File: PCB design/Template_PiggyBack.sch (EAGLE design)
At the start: 46 parts, among them CN1 USB power supply, IC1 MCP6002, IC3 MCP6002, IC4 REG1117

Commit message: PCB Output
changed the PCB Output to PC1 and PC3
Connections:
- removed net PA4: R12.2, TP3.TP
- net PA5: no longer R6.2, TP4.TP
- net PC1_: now also R6.2, TP4.TP
- net PC3: now also R12.2, TP3.TP
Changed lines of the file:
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@@
 <label x="27.94" y="86.36" size="1.778" layer="95"/>
-</segment>
-</net>
-<net name="PC3" class="0">
-<segment>
-<pinref part="J2" gate="G$1" pin="8"/>
-<wire x1="35.56" y1="83.82" x2="33.02" y2="83.82" width="0.1524" layer="91"/>
-<label x="27.94" y="83.82" size="1.778" layer="95"/>
-</segment>
-</net>
-<net name="PA5" class="0">
-<segment>
-<pinref part="J2" gate="G$1" pin="11"/>
-<wire x1="35.56" y1="76.2" x2="33.02" y2="76.2" width="0.1524" layer="91"/>
-<label x="27.94" y="76.2" size="1.778" layer="95"/>
 </segment>
 <segment>
@@
 <wire x1="259.08" y1="-66.04" x2="264.16" y2="-66.04" width="0.1524" layer="91"/>
 <junction x="259.08" y="-66.04"/>
+</segment>
+</net>
+<net name="PC3" class="0">
+<segment>
+<pinref part="J2" gate="G$1" pin="8"/>
+<wire x1="35.56" y1="83.82" x2="33.02" y2="83.82" width="0.1524" layer="91"/>
+<label x="27.94" y="83.82" size="1.778" layer="95"/>
+</segment>
+<segment>
+<pinref part="R12" gate="G$1" pin="2"/>
+<wire x1="256.54" y1="-205.74" x2="261.62" y2="-205.74" width="0.1524" layer="91"/>
+<pinref part="TP3" gate="G$1" pin="TP"/>
+<wire x1="261.62" y1="-205.74" x2="266.7" y2="-205.74" width="0.1524" layer="91"/>
+<junction x="261.62" y="-205.74"/>
+<label x="269.24" y="-205.74" size="1.778" layer="95"/>
+</segment>
+</net>
+<net name="PA5" class="0">
+<segment>
+<pinref part="J2" gate="G$1" pin="11"/>
+<wire x1="35.56" y1="76.2" x2="33.02" y2="76.2" width="0.1524" layer="91"/>
+<label x="27.94" y="76.2" size="1.778" layer="95"/>
 </segment>
 <segment>
@@
 </segment>
 </net>
-<net name="PA4" class="0">
-<segment>
-<pinref part="R12" gate="G$1" pin="2"/>
-<wire x1="256.54" y1="-205.74" x2="261.62" y2="-205.74" width="0.1524" layer="91"/>
-<pinref part="TP3" gate="G$1" pin="TP"/>
-<wire x1="261.62" y1="-205.74" x2="266.7" y2="-205.74" width="0.1524" layer="91"/>
-<junction x="261.62" y="-205.74"/>
-<label x="269.24" y="-205.74" size="1.778" layer="95"/>
-</segment>
-</net>

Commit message: finished layout but it is subject to revision
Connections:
- net VCO: no longer R15.2
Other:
- moved on the sheet: R15
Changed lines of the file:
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@@
 <attribute name="VALUE" x="65.024" y="-134.239" size="1.778" layer="96"/>
 </instance>
-<instance part="R15" gate="G$1" x="81.28" y="-119.38" smashed="yes" rot="R180">
-<attribute name="NAME" x="85.09" y="-120.8786" size="1.778" layer="95" rot="R180"/>
-<attribute name="VALUE" x="85.09" y="-116.078" size="1.778" layer="96" rot="R180"/>
+<instance part="R15" gate="G$1" x="58.42" y="-119.38" smashed="yes" rot="R180">
+<attribute name="NAME" x="62.23" y="-120.8786" size="1.778" layer="95" rot="R180"/>
+<attribute name="VALUE" x="62.23" y="-116.078" size="1.778" layer="96" rot="R180"/>
 </instance>
 <instance part="GND1" gate="1" x="71.12" y="-137.16" smashed="yes">
@@
 <segment>
 <pinref part="R15" gate="G$1" pin="1"/>
-<wire x1="86.36" y1="-119.38" x2="96.52" y2="-119.38" width="0.1524" layer="91"/>
-<label x="96.52" y="-121.92" size="1.778" layer="95"/>
+<wire x1="63.5" y1="-119.38" x2="96.52" y2="-119.38" width="0.1524" layer="91"/>
 </segment>
 </net>
@@
 <pinref part="C17" gate="G$1" pin="1"/>
 <wire x1="71.12" y1="-127" x2="71.12" y2="-119.38" width="0.1524" layer="91"/>
-<pinref part="R15" gate="G$1" pin="2"/>
-<wire x1="71.12" y1="-119.38" x2="76.2" y2="-119.38" width="0.1524" layer="91"/>
-<wire x1="71.12" y1="-119.38" x2="60.96" y2="-119.38" width="0.1524" layer="91"/>
-<junction x="71.12" y="-119.38"/>
-<label x="55.88" y="-119.38" size="1.778" layer="95"/>
-</segment>
-</net>
+</segment>
+</net>

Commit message: better layout version
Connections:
- net PA5: now also R15.2; no longer R15.1
- net VCO: now also R15.1
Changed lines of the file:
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@@
 </segment>
 <segment>
-<pinref part="R15" gate="G$1" pin="1"/>
-<wire x1="63.5" y1="-119.38" x2="96.52" y2="-119.38" width="0.1524" layer="91"/>
+<pinref part="R15" gate="G$1" pin="2"/>
+<wire x1="53.34" y1="-119.38" x2="43.18" y2="-119.38" width="0.1524" layer="91"/>
+<label x="40.64" y="-116.84" size="1.778" layer="95"/>
 </segment>
 </net>
@@
 <pinref part="C17" gate="G$1" pin="1"/>
 <wire x1="71.12" y1="-127" x2="71.12" y2="-119.38" width="0.1524" layer="91"/>
-</segment>
-</net>
+<pinref part="R15" gate="G$1" pin="1"/>
+<wire x1="63.5" y1="-119.38" x2="71.12" y2="-119.38" width="0.1524" layer="91"/>
+<wire x1="71.12" y1="-119.38" x2="81.28" y2="-119.38" width="0.1524" layer="91"/>
+<junction x="71.12" y="-119.38"/>
+<label x="83.82" y="-116.84" size="1.778" layer="95"/>
+</segment>
+</net>

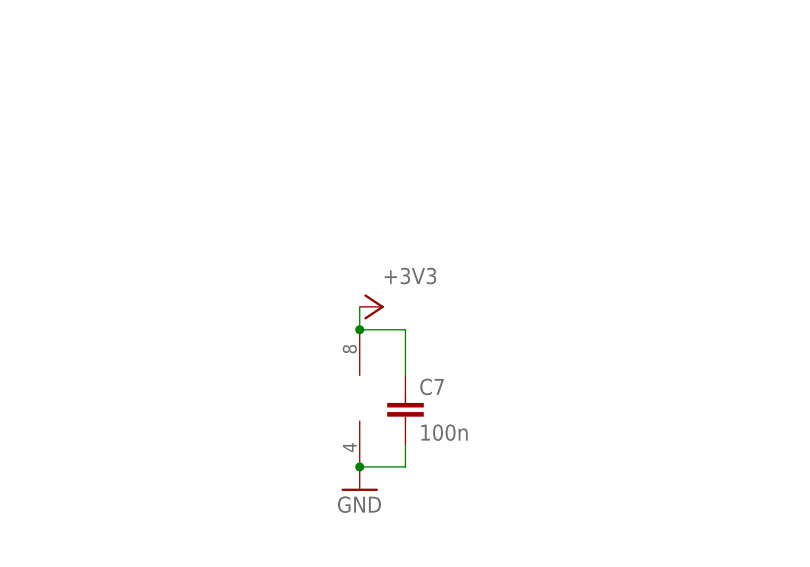
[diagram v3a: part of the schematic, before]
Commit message: errors in layout fixed
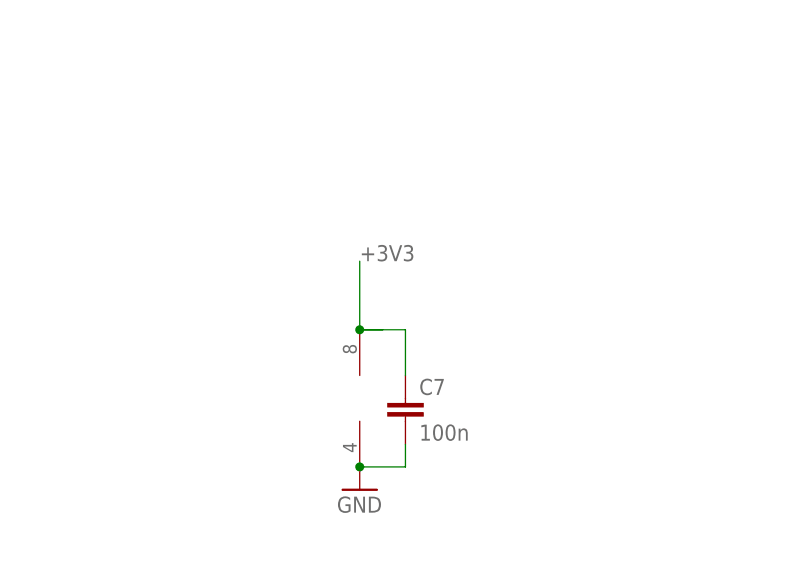
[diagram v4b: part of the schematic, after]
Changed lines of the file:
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@@
 <part name="TP6" library="testpad" library_urn="urn:adsk.eagle:library:385" deviceset="PTR1" device="PAD1-17" package3d_urn="urn:adsk.eagle:package:27949/1"/>
 <part name="+3V3" library="supply1" library_urn="urn:adsk.eagle:library:371" deviceset="+3V3" device=""/>
-<part name="+3V4" library="supply1" library_urn="urn:adsk.eagle:library:371" deviceset="+3V3" device=""/>
 <part name="C17" library="rcl" library_urn="urn:adsk.eagle:library:334" deviceset="C-EU" device="C0805" package3d_urn="urn:adsk.eagle:package:23617/2" value="1u"/>
 <part name="R15" library="rcl" library_urn="urn:adsk.eagle:library:334" deviceset="R-EU_" device="R0805" package3d_urn="urn:adsk.eagle:package:23553/2" value="3k"/>
@@
 <attribute name="VALUE" x="-7.62" y="-154.94" size="1.778" layer="96" rot="R180"/>
 </instance>
-<instance part="+3V4" gate="G$1" x="170.18" y="-27.94" smashed="yes" rot="R270">
-<attribute name="VALUE" x="170.18" y="-25.4" size="1.778" layer="96"/>
-</instance>
 <instance part="C17" gate="G$1" x="71.12" y="-129.54" smashed="yes">
 <attribute name="NAME" x="65.024" y="-129.159" size="1.778" layer="95"/>
@@
 </segment>
 <segment>
+<wire x1="170.18" y1="-162.56" x2="170.18" y2="-165.1" width="0.1524" layer="91"/>
+<label x="170.18" y="-162.56" size="1.778" layer="95"/>
+</segment>
+<segment>
 <pinref part="IC1" gate="P" pin="V+"/>
 <pinref part="C7" gate="G$1" pin="1"/>
 <wire x1="172.72" y1="-35.56" x2="172.72" y2="-30.48" width="0.1524" layer="91"/>
 <wire x1="172.72" y1="-30.48" x2="167.64" y2="-30.48" width="0.1524" layer="91"/>
-<wire x1="167.64" y1="-30.48" x2="167.64" y2="-27.94" width="0.1524" layer="91"/>
+<wire x1="167.64" y1="-30.48" x2="170.18" y2="-30.48" width="0.1524" layer="91"/>
 <junction x="167.64" y="-30.48"/>
-<pinref part="+3V4" gate="G$1" pin="+3V3"/>
-</segment>
-<segment>
-<wire x1="170.18" y1="-162.56" x2="170.18" y2="-165.1" width="0.1524" layer="91"/>
-<label x="170.18" y="-162.56" size="1.778" layer="95"/>
-</segment>
-</net>
+<wire x1="167.64" y1="-30.48" x2="167.64" y2="-22.86" width="0.1524" layer="91"/>
+<label x="167.64" y="-22.86" size="1.778" layer="95"/>
+</segment>
+</net>

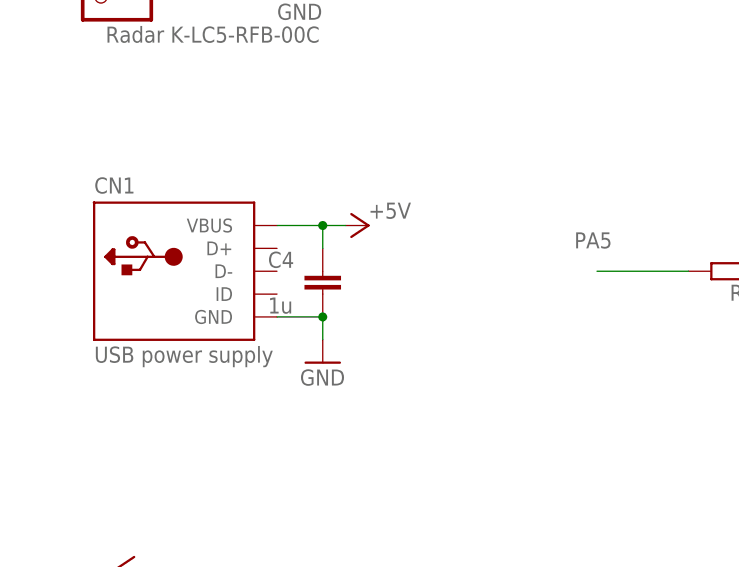
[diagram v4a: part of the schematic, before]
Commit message: adapted layout according to Rennhard's feedback
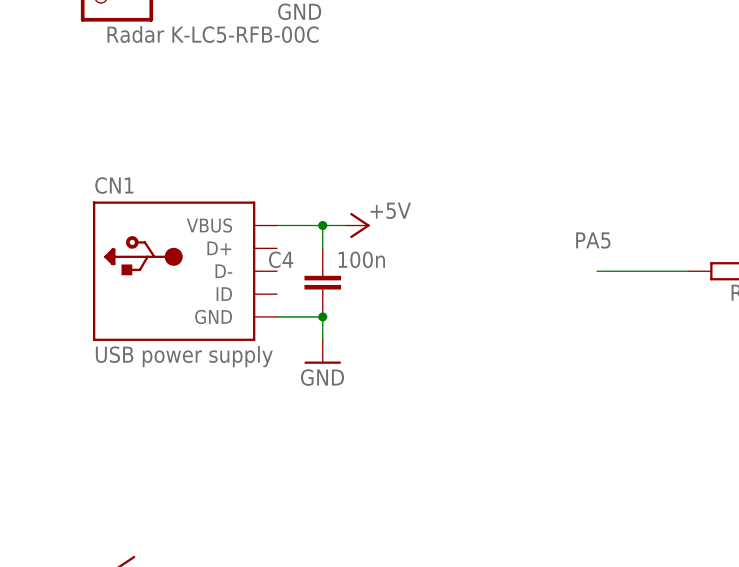
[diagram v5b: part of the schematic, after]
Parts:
- C4: value 1u -> 100n
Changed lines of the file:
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@@
 <part name="GND2" library="supply1" library_urn="urn:adsk.eagle:library:371" deviceset="GND" device=""/>
 <part name="GND3" library="supply1" library_urn="urn:adsk.eagle:library:371" deviceset="GND" device=""/>
-<part name="C4" library="rcl" library_urn="urn:adsk.eagle:library:334" deviceset="C-EU" device="C0805" package3d_urn="urn:adsk.eagle:package:23617/2" value="1u"/>
+<part name="C4" library="rcl" library_urn="urn:adsk.eagle:library:334" deviceset="C-EU" device="C0805" package3d_urn="urn:adsk.eagle:package:23617/2" value="100n"/>
 <part name="JP5" library="pinhead" library_urn="urn:adsk.eagle:library:325" deviceset="PINHD-1X5" device="" package3d_urn="urn:adsk.eagle:package:22469/2" value="Radar K-LC5-RFB-00C"/>
 <part name="GND4" library="supply1" library_urn="urn:adsk.eagle:library:371" deviceset="GND" device=""/>
@@
 <instance part="C4" gate="G$1" x="12.7" y="-119.38" smashed="yes">
 <attribute name="NAME" x="6.604" y="-118.999" size="1.778" layer="95"/>
-<attribute name="VALUE" x="6.604" y="-124.079" size="1.778" layer="96"/>
+<attribute name="VALUE" x="14.224" y="-118.999" size="1.778" layer="96"/>
 </instance>
 <instance part="JP5" gate="A" x="-12.7" y="-83.82" smashed="yes" rot="MR0">

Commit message: errors fixed
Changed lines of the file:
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@@
 <part name="C5" library="rcl" library_urn="urn:adsk.eagle:library:334" deviceset="C-EU" device="C0805" package3d_urn="urn:adsk.eagle:package:23617/2" value="10u"/>
 <part name="C6" library="rcl" library_urn="urn:adsk.eagle:library:334" deviceset="C-EU" device="C0805" package3d_urn="urn:adsk.eagle:package:23617/2" value="10u"/>
-<part name="+3V2" library="supply1" library_urn="urn:adsk.eagle:library:371" deviceset="+3V3" device=""/>
 <part name="P+4" library="supply1" library_urn="urn:adsk.eagle:library:371" deviceset="+5V" device=""/>
 <part name="P+6" library="supply1" library_urn="urn:adsk.eagle:library:371" deviceset="+5V" device=""/>
@@
 <part name="TP5" library="testpad" library_urn="urn:adsk.eagle:library:385" deviceset="PTR1" device="PAD1-17" package3d_urn="urn:adsk.eagle:package:27949/1"/>
 <part name="TP6" library="testpad" library_urn="urn:adsk.eagle:library:385" deviceset="PTR1" device="PAD1-17" package3d_urn="urn:adsk.eagle:package:27949/1"/>
-<part name="+3V3" library="supply1" library_urn="urn:adsk.eagle:library:371" deviceset="+3V3" device=""/>
 <part name="C17" library="rcl" library_urn="urn:adsk.eagle:library:334" deviceset="C-EU" device="C0805" package3d_urn="urn:adsk.eagle:package:23617/2" value="1u"/>
 <part name="R15" library="rcl" library_urn="urn:adsk.eagle:library:334" deviceset="R-EU_" device="R0805" package3d_urn="urn:adsk.eagle:package:23553/2" value="3k"/>
@@
 <attribute name="VALUE" x="21.844" y="-52.959" size="1.778" layer="96"/>
 </instance>
-<instance part="+3V2" gate="G$1" x="25.4" y="-43.18" smashed="yes" rot="R270">
-<attribute name="VALUE" x="22.86" y="-40.64" size="1.778" layer="96"/>
-</instance>
 <instance part="P+4" gate="1" x="17.78" y="-114.3" smashed="yes" rot="MR90">
 <attribute name="VALUE" x="17.78" y="-111.76" size="1.778" layer="96" rot="MR180"/>
@@
 <attribute name="NAME" x="100.076" y="-191.77" size="1.778" layer="95" rot="R270"/>
 <attribute name="TP_SIGNAL_NAME" x="97.79" y="-195.58" size="1.778" layer="97" rot="R180"/>
-</instance>
-<instance part="+3V3" gate="G$1" x="-10.16" y="-152.4" smashed="yes" rot="R90">
-<attribute name="VALUE" x="-7.62" y="-154.94" size="1.778" layer="96" rot="R180"/>
 </instance>
 <instance part="C17" gate="G$1" x="71.12" y="-129.54" smashed="yes">
@@
 <net name="+3V3" class="0">
 <segment>
-<pinref part="IC4" gate="G$1" pin="VOUT"/>
-<pinref part="+3V2" gate="G$1" pin="+3V3"/>
-<wire x1="17.78" y1="-43.18" x2="20.32" y2="-43.18" width="0.1524" layer="91"/>
-<pinref part="C6" gate="G$1" pin="1"/>
-<wire x1="20.32" y1="-43.18" x2="22.86" y2="-43.18" width="0.1524" layer="91"/>
-<wire x1="20.32" y1="-45.72" x2="20.32" y2="-43.18" width="0.1524" layer="91"/>
-<junction x="20.32" y="-43.18"/>
-</segment>
-<segment>
 <pinref part="JP5" gate="A" pin="2"/>
 <wire x1="7.62" y1="-81.28" x2="-10.16" y2="-81.28" width="0.1524" layer="91"/>
 <pinref part="+3V1" gate="G$1" pin="+3V3"/>
-</segment>
-<segment>
-<pinref part="R4" gate="G$1" pin="2"/>
-<wire x1="2.54" y1="-157.48" x2="2.54" y2="-152.4" width="0.1524" layer="91"/>
-<pinref part="+3V3" gate="G$1" pin="+3V3"/>
-<wire x1="-7.62" y1="-152.4" x2="2.54" y2="-152.4" width="0.1524" layer="91"/>
 </segment>
 <segment>
@@
 <label x="167.64" y="-22.86" size="1.778" layer="95"/>
 </segment>
-</net>
+<segment>
+<pinref part="R4" gate="G$1" pin="2"/>
+<wire x1="2.54" y1="-157.48" x2="2.54" y2="-152.4" width="0.1524" layer="91"/>
+<wire x1="-7.62" y1="-152.4" x2="2.54" y2="-152.4" width="0.1524" layer="91"/>
+<label x="-10.16" y="-149.86" size="1.778" layer="95"/>
+</segment>
+<segment>
+<pinref part="IC4" gate="G$1" pin="VOUT"/>
+<wire x1="17.78" y1="-43.18" x2="20.32" y2="-43.18" width="0.1524" layer="91"/>
+<pinref part="C6" gate="G$1" pin="1"/>
+<wire x1="20.32" y1="-43.18" x2="22.86" y2="-43.18" width="0.1524" layer="91"/>
+<wire x1="20.32" y1="-45.72" x2="20.32" y2="-43.18" width="0.1524" layer="91"/>
+<junction x="20.32" y="-43.18"/>
+<label x="22.86" y="-43.18" size="1.778" layer="95"/>
+</segment>
+</net>

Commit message: layout done
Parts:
- added C18: 100n, rcl:C-EUC0805
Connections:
- removed net N$6: C8.1, R4.1, R8.2, TP2.TP
- net +3V3: now also C18.1
- net GND: now also C18.2
- net V_GND: now also C8.1, R4.1, R8.2, TP2.TP
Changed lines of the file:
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@@
 <part name="R15" library="rcl" library_urn="urn:adsk.eagle:library:334" deviceset="R-EU_" device="R0805" package3d_urn="urn:adsk.eagle:package:23553/2" value="3k"/>
 <part name="GND1" library="supply1" library_urn="urn:adsk.eagle:library:371" deviceset="GND" device=""/>
+<part name="C18" library="rcl" library_urn="urn:adsk.eagle:library:334" deviceset="C-EU" device="C0805" package3d_urn="urn:adsk.eagle:package:23617/2" value="100n"/>
 </parts>
 <sheets>
@@
 <attribute name="VALUE" x="68.58" y="-139.7" size="1.778" layer="96"/>
 </instance>
+<instance part="C18" gate="G$1" x="22.86" y="-83.82" smashed="yes">
+<attribute name="NAME" x="16.764" y="-83.439" size="1.778" layer="95"/>
+<attribute name="VALUE" x="24.384" y="-83.439" size="1.778" layer="96"/>
+</instance>
 </instances>
 <busses>
@@
 <segment>
 <pinref part="JP5" gate="A" pin="4"/>
-<wire x1="-10.16" y1="-86.36" x2="10.16" y2="-86.36" width="0.1524" layer="91"/>
+<wire x1="-10.16" y1="-86.36" x2="5.08" y2="-86.36" width="0.1524" layer="91"/>
 <pinref part="GND4" gate="1" pin="GND"/>
+<pinref part="C18" gate="G$1" pin="2"/>
+<wire x1="5.08" y1="-86.36" x2="10.16" y2="-86.36" width="0.1524" layer="91"/>
+<wire x1="22.86" y1="-88.9" x2="15.24" y2="-88.9" width="0.1524" layer="91"/>
+<wire x1="15.24" y1="-88.9" x2="15.24" y2="-83.82" width="0.1524" layer="91"/>
+<wire x1="15.24" y1="-83.82" x2="5.08" y2="-83.82" width="0.1524" layer="91"/>
+<wire x1="5.08" y1="-83.82" x2="5.08" y2="-86.36" width="0.1524" layer="91"/>
+<junction x="5.08" y="-86.36"/>
 </segment>
 <segment>
@@
 <segment>
 <pinref part="JP5" gate="A" pin="2"/>
-<wire x1="7.62" y1="-81.28" x2="-10.16" y2="-81.28" width="0.1524" layer="91"/>
+<wire x1="7.62" y1="-81.28" x2="5.08" y2="-81.28" width="0.1524" layer="91"/>
 <pinref part="+3V1" gate="G$1" pin="+3V3"/>
-</segment>
-<segment>
-<wire x1="170.18" y1="-162.56" x2="170.18" y2="-165.1" width="0.1524" layer="91"/>
-<label x="170.18" y="-162.56" size="1.778" layer="95"/>
+<pinref part="C18" gate="G$1" pin="1"/>
+<wire x1="5.08" y1="-81.28" x2="-10.16" y2="-81.28" width="0.1524" layer="91"/>
+<wire x1="22.86" y1="-81.28" x2="22.86" y2="-76.2" width="0.1524" layer="91"/>
+<wire x1="22.86" y1="-76.2" x2="5.08" y2="-76.2" width="0.1524" layer="91"/>
+<wire x1="5.08" y1="-76.2" x2="5.08" y2="-81.28" width="0.1524" layer="91"/>
+<junction x="5.08" y="-81.28"/>
 </segment>
 <segment>
@@
 <wire x1="170.18" y1="-170.18" x2="170.18" y2="-165.1" width="0.1524" layer="91"/>
 <junction x="170.18" y="-170.18"/>
-</segment>
-</net>
-<net name="N$6" class="0">
+<wire x1="170.18" y1="-162.56" x2="170.18" y2="-165.1" width="0.1524" layer="91"/>
+<label x="170.18" y="-162.56" size="1.778" layer="95"/>
+</segment>
+</net>
+<net name="V_GND" class="0">
+<segment>
+<pinref part="R1" gate="G$1" pin="1"/>
+<wire x1="121.92" y1="-86.36" x2="121.92" y2="-93.98" width="0.1524" layer="91"/>
+<label x="121.92" y="-93.98" size="1.778" layer="95" rot="R180"/>
+</segment>
+<segment>
+<pinref part="R9" gate="G$1" pin="1"/>
+<wire x1="124.46" y1="-226.06" x2="124.46" y2="-233.68" width="0.1524" layer="91"/>
+<label x="124.46" y="-233.68" size="1.778" layer="95" rot="R180"/>
+</segment>
 <segment>
 <pinref part="R4" gate="G$1" pin="1"/>
@@
 <wire x1="33.02" y1="-177.8" x2="40.64" y2="-177.8" width="0.1524" layer="91"/>
 <junction x="33.02" y="-177.8"/>
-</segment>
-</net>
-<net name="V_GND" class="0">
-<segment>
 <label x="40.64" y="-177.8" size="1.778" layer="95"/>
 </segment>
-<segment>
-<pinref part="R1" gate="G$1" pin="1"/>
-<wire x1="121.92" y1="-86.36" x2="121.92" y2="-93.98" width="0.1524" layer="91"/>
-<label x="121.92" y="-93.98" size="1.778" layer="95" rot="R180"/>
-</segment>
-<segment>
-<pinref part="R9" gate="G$1" pin="1"/>
-<wire x1="124.46" y1="-226.06" x2="124.46" y2="-233.68" width="0.1524" layer="91"/>
-<label x="124.46" y="-233.68" size="1.778" layer="95" rot="R180"/>
-</segment>
-</net>
+</net>
